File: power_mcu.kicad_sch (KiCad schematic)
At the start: 46 parts, among them J1 USB-C 16P, J3 FLOW, J4 OUTDOOR, J5 OLED, J6 QWIIC, J7 SPARE, J8 BOOT_JP, SW1 RESET, SW2 BOOT, SW3 BTN1, SW4 BTN2, U1 ESP32-C6-WROOM-1-N8, U2 AMS1117-3.3, U3 USBLC6-2SC6

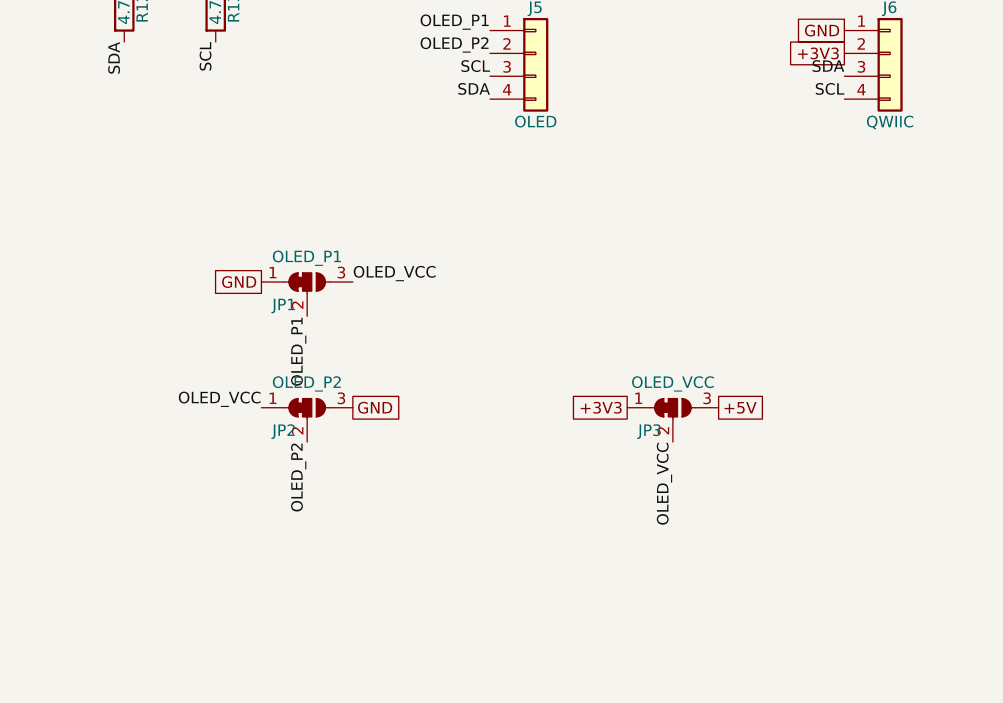
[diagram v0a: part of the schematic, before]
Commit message: Place and autoroute the board; add the reproducible routing pipeline
Board 150 x 95 mm, 2-layer, routed with Freerouting 2.5 from a placed
layout: DRC 0 violations / 0 unconnected, schematic parity clean, ERC clean.

- Isolation band, antenna keep-out, relay/opto slots, 6.4 mm mains-to-SELV
  custom DRC (heating-controller.kicad_dru) and MAINS / MAINS_SENSE / Power
  net classes in the project file.
- Fixed wiring laid before routing: L/N buses, relay COM/NO links,
  DEMAND_RET return, USB-C D+/D- bridges and VBUS escape, 31 GND stitching
  vias so the bottom pour stays in one piece.
- J115/J116 moved in from the board edge so every courtyard is inside the
  outline (JLC assembly margin).
- tools/route/: prep -> Freerouting -> SES import + pours -> DRC + gap fix,
  reproducible in ~2 min; outputs land in fab/route/ (ignored).
- Schematic: pin-type fixes in the project library, ESP32 thermal pads
  numbered; docs/design.md layout section rewritten to match the board.

Co-Authored-By: Claude Fable 5.1 <noreply@anthropic.com>
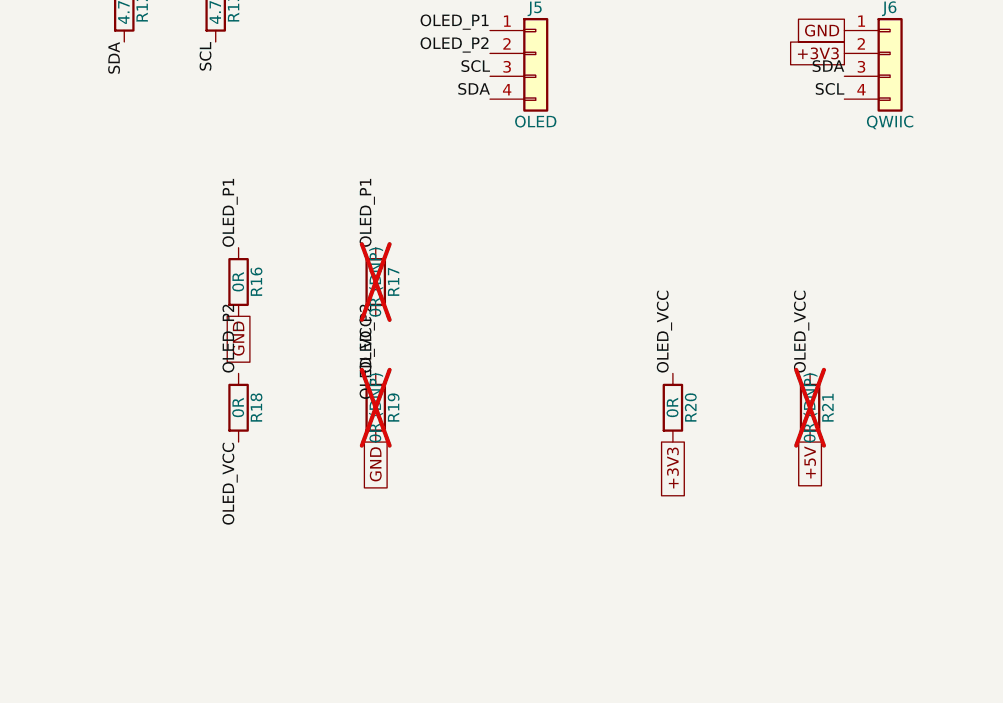
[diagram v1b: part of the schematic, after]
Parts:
- removed JP1: OLED_P1, Jumper:SolderJumper-3_P1.3mm_Bridged12_RoundedPad1.0x1.5mm, symbol Jumper:SolderJumper_3_Bridged12
- removed JP2: OLED_P2, Jumper:SolderJumper-3_P1.3mm_Bridged12_RoundedPad1.0x1.5mm, symbol Jumper:SolderJumper_3_Bridged12
- removed JP3: OLED_VCC, Jumper:SolderJumper-3_P1.3mm_Bridged12_RoundedPad1.0x1.5mm, symbol Jumper:SolderJumper_3_Bridged12
- added R16, R18, R20: 0R, Resistor_SMD:R_0603_1608Metric, symbol Device:R
- added R17, R19, R21: 0R (DNP), Resistor_SMD:R_0603_1608Metric, symbol Device:R
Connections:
- net +3V3: now also R20.2
- net +5V: now also R21.2
- net GND: now also R16.2, R19.2
- net OLED_P1: now also R16.1, R17.1
- net OLED_P2: now also R18.1, R19.1
- net OLED_VCC: now also R17.2, R18.2, R20.1, R21.1

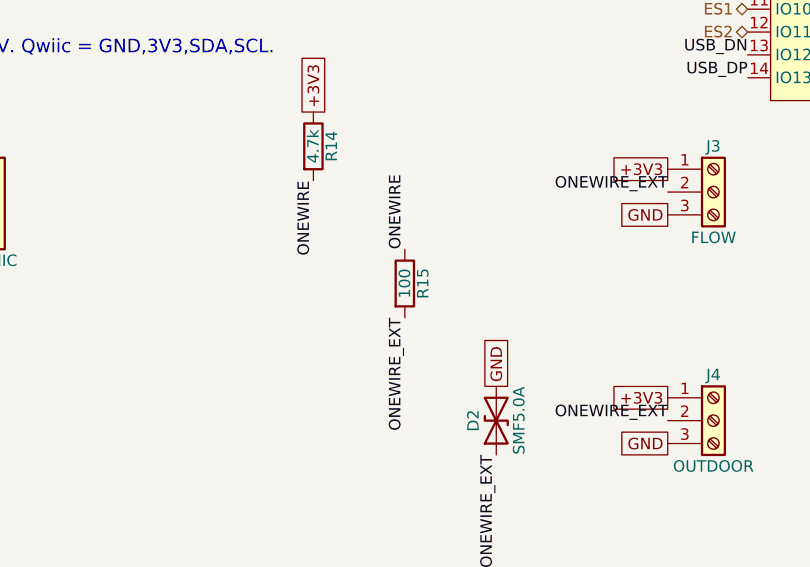
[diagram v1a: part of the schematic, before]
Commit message: Address the independent design review: OT net split and fuse, 2.0 mm live-input class, demand detector margin, 3V3 copper, silkscreen
Two review rounds closed with design changes rather than prose:

- OpenTherm: U201 emitter and D207 cathode moved off OT_N1 onto OT_TXE
  (the net merge echoed our own TX into the RX opto); D208 SMAJ24A fitted;
  F201 1 A 250 V fast 2410 fuse in series with OT1 so a 230 V miswire is a
  calculable TVS-plus-fuse crowbar instead of parts failing open.
- Raw live inputs (ES1-3_IN, DEMAND_230) in a MAINS_IN class at 2.0 mm to
  everything, included in the 6.4 mm and edge rules; mains-to-mains 2.0 mm;
  the four inputs are pre-routed as locked lanes (the autorouter cannot
  thread them at that clearance); J115 wired ES3/ES2/ES1 top to bottom.
- Demand chain 3+3 and opto pull-ups 220 k after a time-domain model showed
  the 24 V detector had no margin; R15 330 R limits 1-Wire clamp current.
- +3V3 copper on the regulator tab (locked bars + pour, 125 mm2); GND island
  repair vias and stitching cleanup in the pipeline; silkscreen labels at
  every terminal pin plus warnings; LCSC/Description/Datasheet copied into
  the PCB footprints so schematic parity is clean (7 board-only items).
- Docs: design.md and requirements.md corrected where they had drifted;
  docs/layout-notes.md records what worked and failed in routing and margins.

Board: DRC 0 errors / 0 unconnected, ERC 0 errors, courtyards inside the
outline, Freerouting 40 passes in ~1 min.

Co-Authored-By: Claude Fable 5.1 <noreply@anthropic.com>
Claude-Session: https://claude.ai/code/session_01XDSh2Z4phxf7z2Gu1153CL
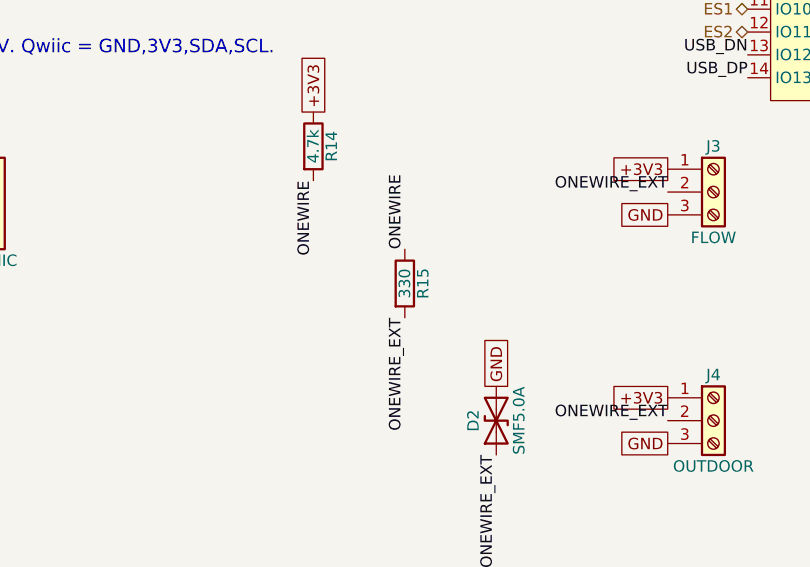
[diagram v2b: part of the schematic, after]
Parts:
- R15: value 100 -> 330; LCSC C22775 -> C23138
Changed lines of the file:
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@@
 			)
 		)
-		(property "Value" "100"
+		(property "Value" "330"
 			(at 180.34 175.26 90)
 			(effects
@@
 			)
 		)
-		(property "LCSC" "C22775"
+		(property "LCSC" "C23138"
 			(at 180.34 175.26 0)
 			(hide yes)

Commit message: Name the board Andiron v1.0; add BOM with cost estimates, renders, getting-started docs and CLAUDE.md
- Andiron v1.0 and the author name on the silkscreen, in every title block
  and in the README; J116 warning moved inside the board edge.
- tools/bom.py: BOM from the schematic with LCSC prices from the Konnect
  JLCPCB database -> docs/BOM.md (cost summary, Basic/Extended, DNP list) and
  docs/bom/andiron-bom-jlc.csv (JLCPCB upload). ~$15.77 components per board,
  ~$28.97 per board at 5 including assumed Extended-part fees.
- tools/sync_models.py relinks all 152 footprints to 3D models with portable
  ${KIPRJMOD} paths (also fixed in lib/jlc.pretty); stand-ins for the
  ESP32-C6 module and HRO USB-C. Wired into the routing pipeline.
- tools/render.sh: ray-traced 3D views and 2D layer plots in docs/images/.
- README rewritten: renders, BOM summary, getting started with Konnect MCP,
  repository layout. tools/README.md indexes every script; Konnect helpers
  and the pour-island check moved into tools/.
- CLAUDE.md: BOM and cost estimate kept current on every schematic change,
  definition of done for board changes.
- .konnect/project.json design rules brought in line with what is built;
  project-local .mcp.json for Konnect.
- Removed references to a commercial product; the docs now describe the
  board on its own terms, designed for Home Assistant and ESPHome.

ERC 0 errors; DRC 0 errors, 0 unconnected, parity clean.

Co-Authored-By: Claude Opus 5.5 <noreply@anthropic.com>
Claude-Session: https://claude.ai/code/session_01XDSh2Z4phxf7z2Gu1153CL
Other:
- company: (none) -> Cedric Van Goethem
- title: (none) -> Andiron
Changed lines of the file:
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@@
 	(generator_version "10.0")
 	(paper "A3")
+	(title_block
+		(title "Andiron")
+		(date "2026-10-22")
+		(rev "v1.0")
+		(company "Cedric Van Goethem")
+	)
 	(no_connect
 		(at 64.77 92.71)

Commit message: Andiron v1.0 redesign: volt-free changeover relays, no mains sensing, layout by module area
- Relays: four HF115F/005-1ZS3A changeover relays (CH1-CH4), each with its own
  NC/COM/NO terminal, as UK heating controllers present their outputs; 5 kV
  VDE-reinforced coil-to-contact insulation. Each channel is its own net class
  and keeps 6.4 mm clearance and creepage from everything that is not itself.
- Removed the 230 V supply input, L/N rails and all five mains sensing inputs
  (30 resistors, 5 optos, end-switch and demand terminals). The only mains on
  the board is the relay contacts.
- Power: LDL1117S33R replaces the AMS1117 (0.35 V dropout, ceramic-stable,
  18 V abs-max, no heat-spreading copper); relays run from USB 5 V directly.
- OLED header fixed to GND/3V3/SCL/SDA (option resistors removed); freed GPIOs
  on an 8-pin spare header; Mains IO sheet renamed Relays.
- Layout regenerated by module area (relay strip, drivers, MCU with antenna at
  the left edge, power, OpenTherm, sensors, controls), 150 x 90 mm. Placement
  and shared geometry now in tools/layout/; tools/sync_netlist.py syncs the
  schematic to the board headlessly.
- Low-voltage clearance 0.25 mm so module pins escape straight out; USB nets
  get their own 0.2 mm class. Pipeline widens router neck-down stubs; stitching
  and island-repair vias avoid pads.
- Silkscreen relabelled in plain language (CH1 NC COM NO, OPENTHERM, FLOW TEMP,
  OUTDOOR TEMP, ...); repository URL removed.
- Docs: requirements and design brief rewritten for v1.0, schematic plan,
  README, BOM, renders, schematic PDF and layout lessons updated.

ERC 0 errors; DRC 0 errors, 0 unconnected, parity clean; sanity PASS.
BOM: ~$15.77 -> ~$24.03 components per board (~$28.97 -> ~$37.23 at 5 incl.
fees), mostly the four HF115F relays.

Co-Authored-By: Claude Opus 5.5 <noreply@anthropic.com>
Claude-Session: https://claude.ai/code/session_01XDSh2Z4phxf7z2Gu1153CL
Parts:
- removed J7: SPARE, Connector_PinHeader_2.54mm:PinHeader_1x04_P2.54mm_Vertical, symbol Connector_Generic:Conn_01x04
- removed R16, R18, R20: 0R, Resistor_SMD:R_0603_1608Metric, symbol Device:R
- removed R17, R19, R21: 0R (DNP), Resistor_SMD:R_0603_1608Metric, symbol Device:R
- added J7: SPARE GPIO, Connector_PinHeader_2.54mm:PinHeader_1x08_P2.54mm_Vertical, symbol Connector_Generic:Conn_01x08
- J5: value OLED -> OLED GND/3V3/SCL/SDA
- U2: value AMS1117-3.3 -> LDL1117S33R; LCSC C6186 -> C435835
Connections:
- net OLED_P1 is gone; now on net GND: J5.1 (Pin_1)
- net OLED_P2 is gone; now on net +3V3: J5.2 (Pin_2)
- net +3V3: now also J7.7 (Pin_7)
- net GND: now also J7.8 (Pin_8)
- net SPARE16: now also J7.1 (Pin_1)
- net SPARE17: now also J7.2 (Pin_2)
- net DEMAND_IN renamed IO19
- net IO19: now also J7.6 (Pin_6)
- net ES1 renamed IO10
- net IO10: now also J7.3 (Pin_3)
- net ES2 renamed IO11
- net IO11: now also J7.4 (Pin_4)
- net ES3 renamed IO18
- net IO18: now also J7.5 (Pin_5)
- net MAINS_OK: no longer names the net of U1.18 (IO20)
- no-connect marks 3 -> 4
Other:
- note added: "OLED header J5: GND, 3V3, SCL, SDA (standard 4-pin I2C OLED modules). Qwiic J6: GND, 3V3, SDA, SCL. Spare J7: IO16, IO17, IO10, IO11, IO18, IO19, 3V3, GND."
- note removed: "OLED header: JP1/JP2 select pin-1/2 order (GND,VCC default). JP3 selects OLED VCC 3V3 (default) or 5V. Qwiic = GND,3V3,SDA,SCL."

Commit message: Wall-hanging layout, cheaper parts, OLED area
Layout (160 x 95 mm): the board hangs on a wall with every cable from below
or the left. Relay and OpenTherm terminals on the bottom edge, USB-C, FLOW,
OUTDOOR and Qwiic on the left edge, antenna at the top edge. The OLED module
stacks in landscape over a reserved top-right area.

Parts: TE RT314005 relays replace the HF115F (same body and pin grid,
reinforced 5 kV / 10 mm insulation, flux-proof so no washing after THT); AEM
MF2410F1.000TM fast fuse replaces the Bourns (same breaking capacity and
I2t, Bourns nearly out of stock); Basic 100 nF and 1 uF capacitors.
Per-board total at 5: $37.23 -> $27.86 (components $24.03 -> $15.86).

Tooling: locked +5V rail and supply feed (Freerouting would not route the
net), USB-C pre-routes drawn in the receptacle's own frame, router keep-outs
over the isolation slots, temporary zones stripped in a text pass, wider
pour-island repair, a pre-routing placement check, and sanity checks for
connector edges, no-cable edges and the OLED area.

Co-Authored-By: Claude Opus 5.5 <noreply@anthropic.com>
Claude-Session: https://claude.ai/code/session_01XDSh2Z4phxf7z2Gu1153CL
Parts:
- C10, C5, C7, C9: LCSC C1591 -> C14663
- C8: LCSC C5673 -> C15849
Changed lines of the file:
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@@
 			)
 		)
-		(property "LCSC" "C1591"
+		(property "LCSC" "C14663"
 			(at 199.39 59.69 0)
 			(hide yes)
@@
 			)
 		)
-		(property "LCSC" "C1591"
+		(property "LCSC" "C14663"
 			(at 299.72 59.69 0)
 			(hide yes)
@@
 			)
 		)
-		(property "LCSC" "C5673"
+		(property "LCSC" "C15849"
 			(at 330.2 59.69 0)
 			(hide yes)
@@
 			)
 		)
-		(property "LCSC" "C1591"
+		(property "LCSC" "C14663"
 			(at 330.2 110.49 0)
 			(hide yes)
@@
 			)
 		)
-		(property "LCSC" "C1591"
+		(property "LCSC" "C14663"
 			(at 330.2 134.62 0)
 			(hide yes)

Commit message: JLC package, placement corrections, Preferred-part swaps
- tools/fab.sh builds the JLCPCB package in fab/jlc/: Gerbers and drill
  zip, BOM copy and a placement file from tools/cpl.py.
- tools/cpl.py applies JLC's orientation conventions per footprint
  (SOT-23/SOT-223 180°, SOT-23-6 -90°, pin headers 90° at the pad centre,
  USB-C at the pad centre), each checked in JLC's placement viewer.
- D1/D2 (SMF5.0A), D208 (SMAJ24A) and D205-D207 (BZT52) moved to the same
  part types from JLC's Preferred library: no Extended-part fee on Economic
  assembly. Datasheets checked; footprints unchanged, no rerouting.
- TVS descriptions corrected to unidirectional.
- bom.py no longer charges the fee on Preferred parts.
- Cost at 5 boards incl. fees: $27.86 -> $24.79 per board estimate; JLC
  quote for 2 assembled boards $104.09 -> $87.98.
- Renders and schematic PDF regenerated; JLC upload lessons in
  layout-notes.

Co-Authored-By: Claude Opus 5.5 <noreply@anthropic.com>
Claude-Session: https://claude.ai/code/session_01XDSh2Z4phxf7z2Gu1153CL
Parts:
- D1, D2: LCSC C193402 -> C19077497
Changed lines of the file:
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@@
 			)
 		)
-		(property "Description" "Bidirectional transient-voltage-suppression diode"
+		(property "Description" "Unidirectional transient-voltage-suppression diode, cathode (pin 1) on the protected rail"
 			(at 85.09 124.46 0)
 			(hide yes)
@@
 			)
 		)
-		(property "LCSC" "C193402"
+		(property "LCSC" "C19077497"
 			(at 85.09 124.46 0)
 			(hide yes)
@@
 			)
 		)
-		(property "Description" "Bidirectional transient-voltage-suppression diode"
+		(property "Description" "Unidirectional transient-voltage-suppression diode, cathode (pin 1) on the protected rail"
 			(at 190.5 190.5 0)
 			(hide yes)
@@
 			)
 		)
-		(property "LCSC" "C193402"
+		(property "LCSC" "C19077497"
 			(at 190.5 190.5 0)
 			(hide yes)

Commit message: OLED on a Qwiic cable, boot jumper removed, enclosure re-sized
- J5 (OLED) is a Qwiic socket, same part as J6, in Qwiic order GND / 3V3 /
  SDA / SCL on GPIO6/GPIO7 (hardware I2C). The module sits in the cover
  window on a short cable (JST-SH to Dupont, or a soldered pigtail); the
  2.9 mm socket replaces a header that needed ~20 mm with Dupont housings.
- J8 (boot jumper) removed from schematic and board: the BOOT button does
  the same.
- Enclosure section rewritten: ~170 x 135 x 32 mm with a mains wiring bay
  (cable clamps, OT/mains rib), standoffs and support posts, USB-C wall
  relief, lid plungers for BTN1/BTN2.
- route_board.py no longer drops a stitching via that a GND track ends on
  (it disconnected a route after this re-route).
- Board re-routed; ERC/DRC/parity/sanity clean. 15 -> 13 Extended parts;
  estimate at 5 boards incl. fees $24.79 -> $23.76 per board.

Co-Authored-By: Claude Opus 5.5 <noreply@anthropic.com>
Claude-Session: https://claude.ai/code/session_01XDSh2Z4phxf7z2Gu1153CL
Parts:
- removed J8: BOOT_JP, Connector_PinHeader_2.54mm:PinHeader_1x02_P2.54mm_Vertical, symbol Connector_Generic:Conn_01x02
- J5: value OLED GND/3V3/SCL/SDA -> OLED (Qwiic) GND/3V3/SDA/SCL; footprint Connector_PinHeader_2.54mm:PinHeader_1x04_P2.54mm_Vertical -> Connector_JST:JST_SH_SM04B-SRSS-TB_1x04-1MP_P1.00mm_Horizontal; LCSC C2691448 -> C160404
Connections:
- net SCL: now also J5.4 (Pin_4); no longer J5.3 (Pin_3)
- net SDA: now also J5.3 (Pin_3); no longer J5.4 (Pin_4)
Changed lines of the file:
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@@
 		)
 	)
-	(label "BOOT"
-		(at 373.38 85.09 180)
-		(effects
-			(font
-				(size 1.27 1.27)
-			)
-			(justify right bottom)
-		)
-	)
 	(label "BTN1"
 		(at 320.04 114.3 270)
@@
 		)
 	)
-	(label "SCL"
+	(label "SDA"
 		(at 90.17 167.64 180)
 		(effects
@@
 		)
 	)
-	(label "SDA"
+	(label "SCL"
 		(at 90.17 170.18 180)
 		(effects
@@
 		)
 	)
-	(global_label "GND"
-		(shape passive)
-		(at 373.38 87.63 180)
-		(effects
-			(font
-				(size 1.27 1.27)
-			)
-			(justify right)
-		)
-	)
 	(global_label "+3V3"
 		(shape passive)
@@
 	)
 	(symbol
-		(lib_id "Connector_Generic:Conn_01x02")
-		(at 378.46 85.09 0)
-		(unit 1)
-		(in_bom yes)
-		(on_board yes)
-		(dnp no)
-		(property "Reference" "J8"
-			(at 378.46 82.55 0)
-			(effects
-				(font
-					(size 1.27 1.27)
-				)
-			)
-		)
-		(property "Value" "BOOT_JP"
-			(at 378.46 90.17 0)
-			(effects
-				(font
-					(size 1.27 1.27)
-				)
-			)
-		)
-		(property "Footprint" "Connector_PinHeader_2.54mm:PinHeader_1x02_P2.54mm_Vertical"
-			(at 378.46 85.09 0)
-			(hide yes)
-			(effects
-				(font
-					(size 1.27 1.27)
-				)
-			)
-		)
-		(property "Datasheet" ""
-			(at 378.46 85.09 0)
-			(hide yes)
-			(effects
-				(font
-					(size 1.27 1.27)
-				)
-			)
-		)
-		(property "Description" "Generic connector, single row, 01x02, script generated (kicad-library-utils/schlib/autogen/connector/)"
-			(at 378.46 85.09 0)
-			(hide yes)
-			(effects
-				(font
-					(size 1.27 1.27)
-				)
-			)
-		)
-		(property "LCSC" "C492401"
-			(at 378.46 85.09 0)
-			(hide yes)
-			(effects
-				(font
-					(size 1.27 1.27)
-				)
-			)
-		)
-		(instances
-			(project "heating-controller"
-				(path "/23b12b18-7422-4c89-b4f7-c26e3f08412d/f602d427-af24-4a8b-a8af-8f2deb33ae4a"
-					(reference "J8")
-					(unit 1)
-				)
-			)
-		)
-	)
-	(symbol
 		(lib_id "Device:R")
 		(at 320.04 110.49 0)
@@
 			)
 		)
-		(property "Value" "OLED GND/3V3/SCL/SDA"
+		(property "Value" "OLED (Qwiic) GND/3V3/SDA/SCL"
 			(at 95.25 172.72 0)
 			(effects
@@
 			)
 		)
-		(property "Footprint" "Connector_PinHeader_2.54mm:PinHeader_1x04_P2.54mm_Vertical"
+		(property "Footprint" "Connector_JST:JST_SH_SM04B-SRSS-TB_1x04-1MP_P1.00mm_Horizontal"
 			(at 95.25 165.1 0)
 			(hide yes)
@@
 			)
 		)
-		(property "LCSC" "C2691448"
+		(property "LCSC" "C160404"
 			(at 95.25 165.1 0)
 			(hide yes)
